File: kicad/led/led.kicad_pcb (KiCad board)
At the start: 2 copper layers, 38.1 x 38.1 mm, 4 parts

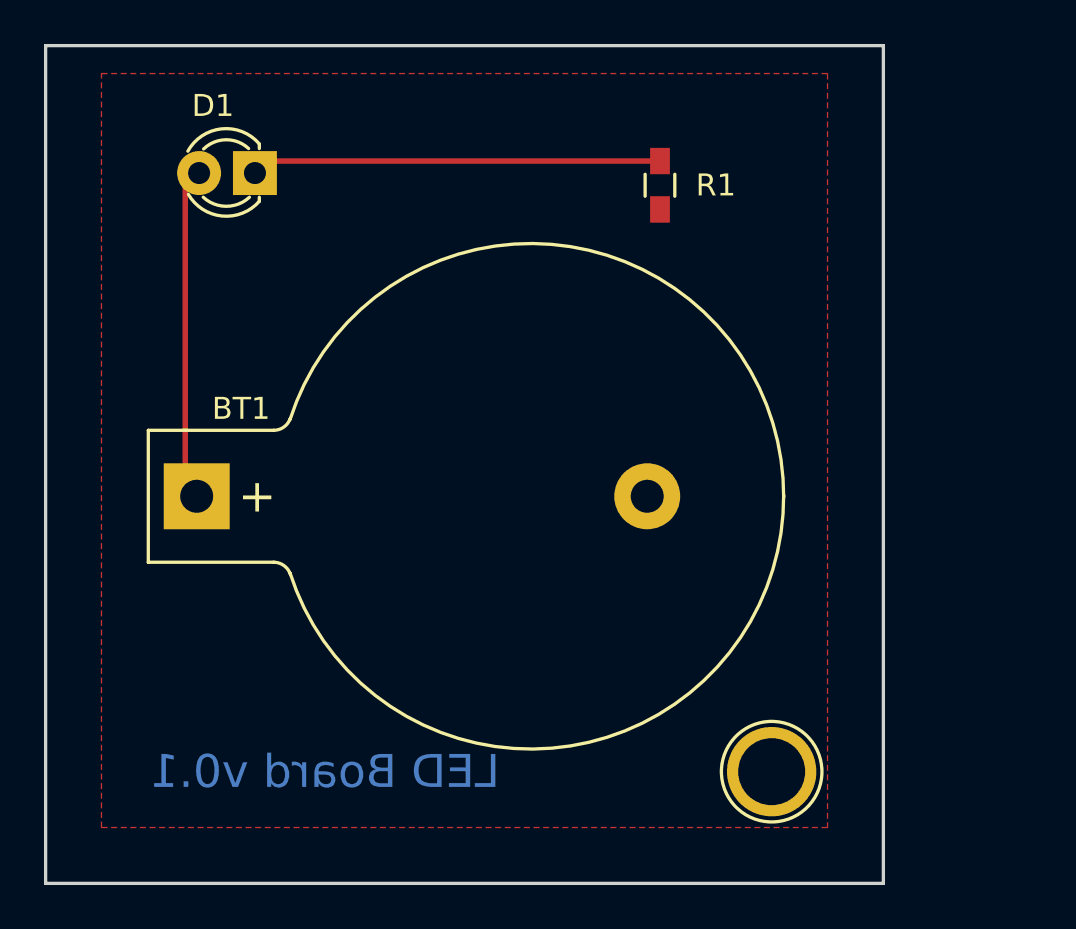
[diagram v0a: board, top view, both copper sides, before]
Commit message: make it compatible with kicad recent version
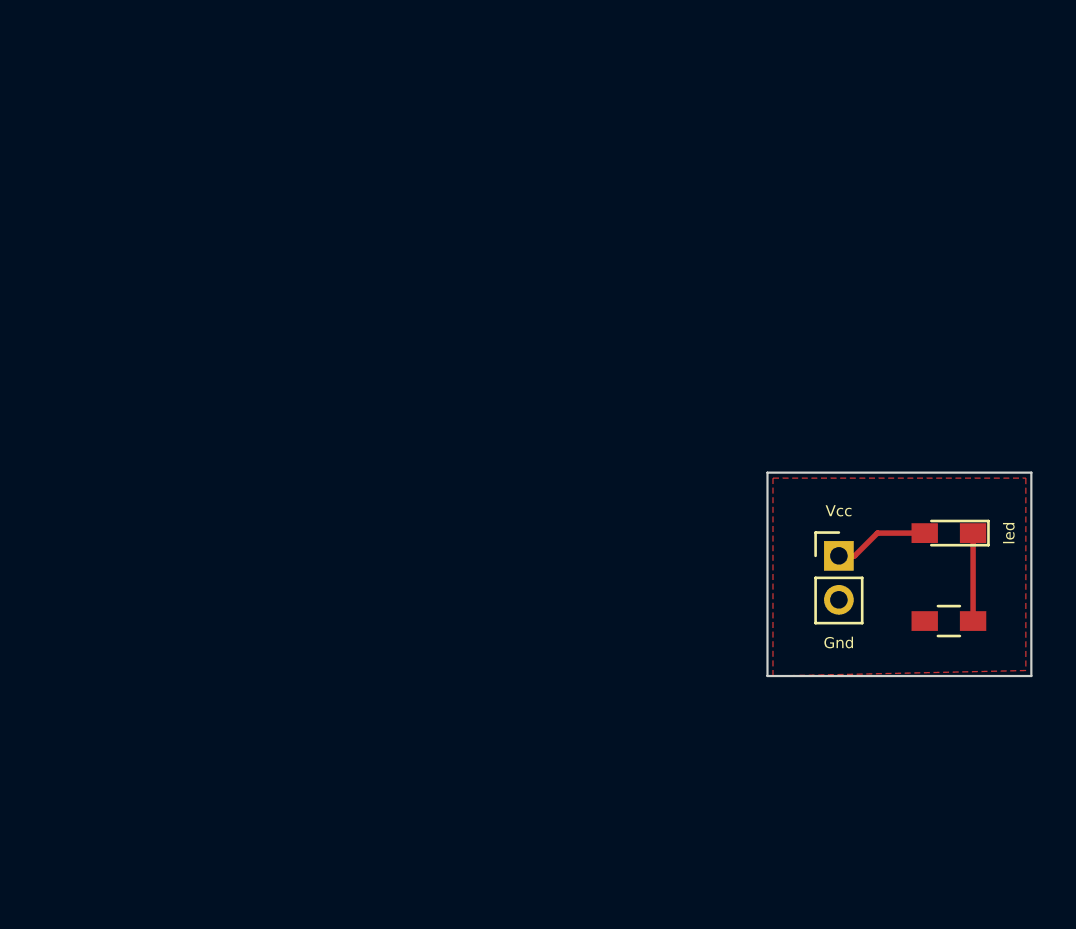
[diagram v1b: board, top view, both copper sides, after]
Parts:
- removed BT1: Battery, Battery_Holders:Keystone_103_1x20mm-CoinCell
- removed D1: LED, LEDs:LED-3MM
- removed REF**: 1pin, Connectors:1pin
- added J1: Conn_01x02, Pin_Headers:Pin_Header_Straight_1x02_Pitch2.00mm, F.Cu at (158.0, 91.8)
- added led: LED, LEDs:LED_0603_HandSoldering, F.Cu at (163.0, 90.8)
- R1: value 100 -> R
- moved R1 23.8 mm to (163.0, 94.8), turned to 180 degrees
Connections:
- R1 pad 1: GND -> Net-(D1-Pad1)
- R1 pad 2: Net-(D1-Pad1) -> GND
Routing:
- net +5V: track 16.7 -> 0.00 mm
- net Net-(D1-Pad1): track 20.7 -> 4.00 mm
- net VCC: track 0.00 -> 4.33 mm
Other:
- board size 38.1 x 38.1 mm -> 12 x 9.2 mm
- net class Default: via_dia 0.8 -> 0.6
- rule pad_to_mask_clearance: 0.2 -> 0
- board text added: "Gnd"
- board text added: "Vcc"
- board text removed: "LED Board v0.1"
